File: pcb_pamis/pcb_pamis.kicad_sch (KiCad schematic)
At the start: 39 parts, among them J10 Conn_01x03, J11 Conn_01x03, J12 Conn_02x06_Odd_Even, J13 USB_C_Receptacle_USB2.0_14P, J2 1755736, J6 Conn_01x05, J7 Conn_01x05, J8 Conn_01x05, J9 Conn_01x03, Q1 Q_NPN_BEC, Q2 Q_NPN_BEC, SW1 SW_Push, U1 ESP32-WROOM-32UE, U2 CP2102N-Axx-xQFN28

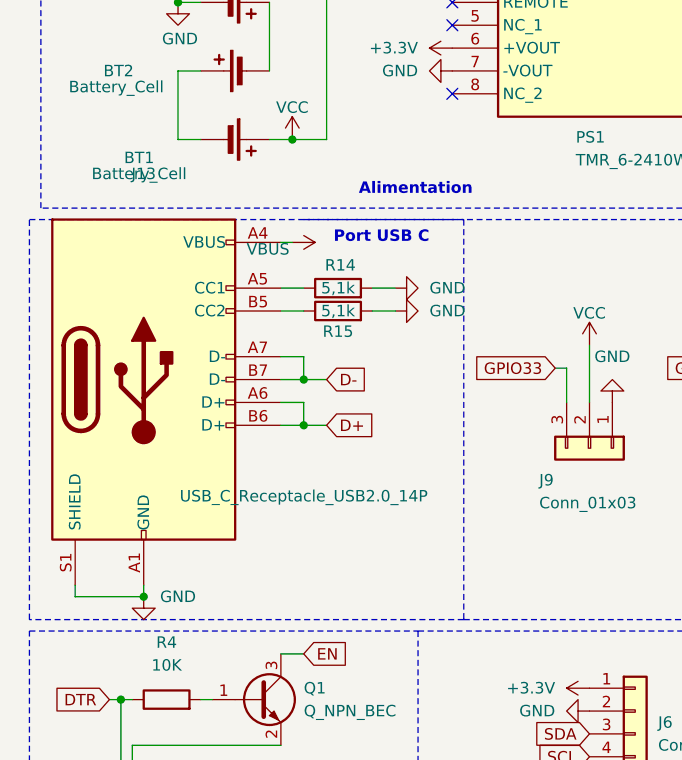
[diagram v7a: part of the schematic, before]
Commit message: correction symbole type C
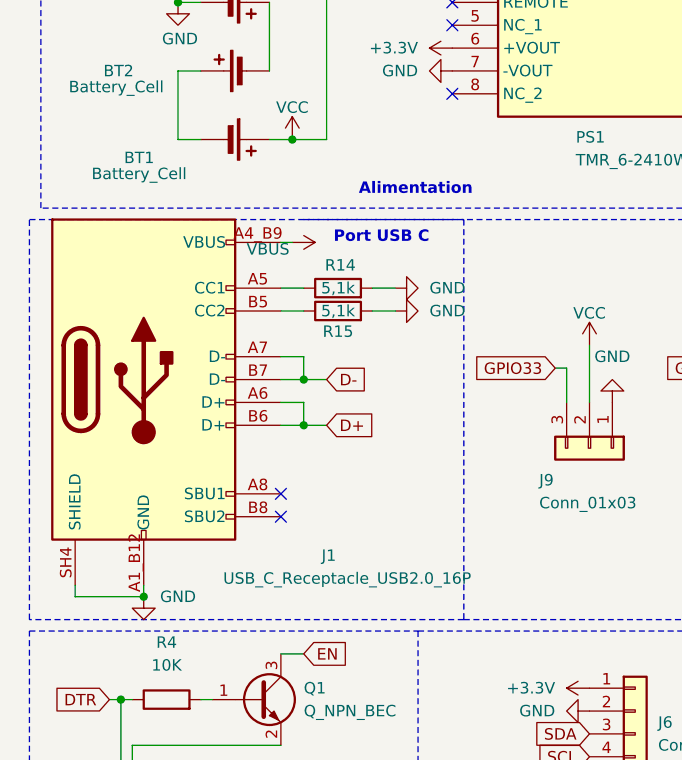
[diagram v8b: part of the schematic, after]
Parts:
- removed J13: USB_C_Receptacle_USB2.0_14P, Modelec:GCT_USB4105-GF-A, symbol Connector:USB_C_Receptacle_USB2.0_14P
- added J1: USB_C_Receptacle_USB2.0_16P, Modelec:GCT_USB4105-GF-A, symbol Modelec:USB_C_Receptacle_USB2.0_16P
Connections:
- net D+: now also J1.A6 (D+), J1.B6 (D+)
- net D-: now also J1.A7 (D-), J1.B7 (D-)
- net GND: now also J1.A1_B12 (GND), J1.B1_A12 (GND), J1.SH1 (SHIELD), J1.SH2 (SHIELD), J1.SH3 (SHIELD), J1.SH4 (SHIELD)
- net VBUS: now also J1.A4_B9 (VBUS), J1.B4_A9 (VBUS)
- net at R15.1: now also J1.B5 (CC2)
- net at R14.1: now also J1.A5 (CC1)
- no-connect marks 22 -> 24
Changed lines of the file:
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@@
 	)
 	(no_connect
+		(at 41.91 87.63)
+	)
+	(no_connect
 		(at 264.16 59.69)
 	)
@@
 	)
 	(no_connect
+		(at 41.91 85.09)
+	)
+	(no_connect
 		(at 139.7 53.34)
 	)
@@
 	)
 	(symbol
+		(lib_id "Modelec:USB_C_Receptacle_USB2.0_16P")
+		(at 26.67 72.39 0)
+		(unit 1)
+		(exclude_from_sim no)
+		(in_bom yes)
+		(on_board yes)
+		(dnp no)
+		(property "Reference" "J1"
+			(at 47.244 91.948 0)
+			(effects
+				(font
+					(size 1.27 1.27)
+				)
+			)
+		)
+		(property "Value" "USB_C_Receptacle_USB2.0_16P"
+			(at 49.276 94.488 0)
+			(effects
+				(font
+					(size 1.27 1.27)
+				)
+			)
+		)
+		(property "Footprint" "Modelec:GCT_USB4105-GF-A"
+			(at 30.48 72.39 0)
+			(effects
+				(font
+					(size 1.27 1.27)
+				)
+				(hide yes)
+			)
+		)
+		(property "Datasheet" "https://www.usb.org/sites/default/files/documents/usb_type-c.zip"
+			(at 30.48 72.39 0)
+			(effects
+				(font
+					(size 1.27 1.27)
+				)
+				(hide yes)
+			)
+		)
+		(property "Description" "USB 2.0-only 16P Type-C Receptacle connector"
+			(at 26.67 72.39 0)
+			(effects
+				(font
+					(size 1.27 1.27)
+				)
+				(hide yes)
+			)
+		)
+		(pin "B6"
+		)
+		(pin "A8"
+		)
+		(pin "A4_B9"
+		)
+		(pin "B4_A9"
+		)
+		(pin "B5"
+		)
+		(pin "SH1"
+		)
+		(pin "A1_B12"
+		)
+		(pin "A6"
+		)
+		(pin "B1_A12"
+		)
+		(pin "A5"
+		)
+		(pin "B7"
+		)
+		(pin "A7"
+		)
+		(pin "B8"
+		)
+		(pin "SH2"
+		)
+		(pin "SH4"
+		)
+		(pin "SH3"
+		)
+		(instances
+			(project ""
+				(path "/cd04cd30-6b87-4bc2-a277-438dac0065f3"
+					(reference "J1")
+					(unit 1)
+				)
+			)
+		)
+	)
+	(symbol
 		(lib_id "Device:C")
 		(at 20.32 153.67 0)
@@
 					(unit 1)
 				)
-			)
-		)
-	)
-	(symbol
-		(lib_id "Connector:USB_C_Receptacle_USB2.0_14P")
-		(at 26.67 72.39 0)
-		(unit 1)
-		(exclude_from_sim no)
-		(in_bom yes)
-		(on_board yes)
-		(dnp no)
-		(property "Reference" "J13"
-			(at 26.67 49.53 0)
-			(effects
-				(font
-					(size 1.27 1.27)
-				)
-			)
-		)
-		(property "Value" "USB_C_Receptacle_USB2.0_14P"
-			(at 44.45 85.344 0)
-			(effects
-				(font
-					(size 1.27 1.27)
-				)
-			)
-		)
-		(property "Footprint" "Modelec:GCT_USB4105-GF-A"
-			(at 30.48 72.39 0)
-			(effects
-				(font
-					(size 1.27 1.27)
-				)
-				(hide yes)
-			)
-		)
-		(property "Datasheet" "https://www.usb.org/sites/default/files/documents/usb_type-c.zip"
-			(at 30.48 72.39 0)
-			(effects
-				(font
-					(size 1.27 1.27)
-				)
-				(hide yes)
-			)
-		)
-		(property "Description" "USB 2.0-only 14P Type-C Receptacle connector"
-			(at 26.67 72.39 0)
-			(effects
-				(font
-					(size 1.27 1.27)
-				)
-				(hide yes)
-			)
-		)
-		(pin "B9"
-		)
-		(pin "S1"
-		)
-		(pin "A12"
-		)
-		(pin "B5"
-		)
-		(pin "B6"
-		)
-		(pin "A4"
-		)
-		(pin "B12"
-		)
-		(pin "A5"
-		)
-		(pin "A9"
-		)
-		(pin "A6"
-		)
-		(pin "B4"
-		)
-		(pin "B1"
-		)
-		(pin "A7"
-		)
-		(pin "A1"
-		)
-		(pin "B7"
-		)
-		(instances
-			(project ""
-				(path "/cd04cd30-6b87-4bc2-a277-438dac0065f3"
-					(reference "J13")
-					(unit 1)
-				)
